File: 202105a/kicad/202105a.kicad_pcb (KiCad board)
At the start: 2 copper layers, 16 parts, among them J101 PWR, J102 IN, J103 OUT, J104 GAIN, U101 LM386

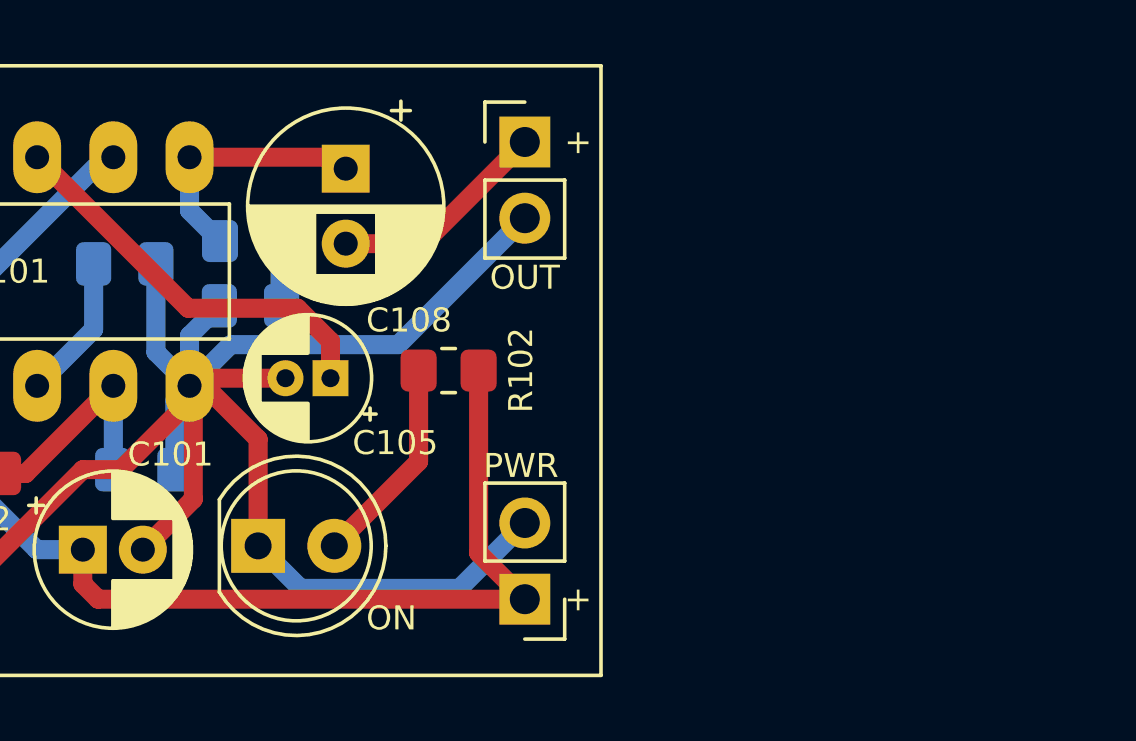
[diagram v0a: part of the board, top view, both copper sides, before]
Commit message: 添加输出插座，并移动了LED
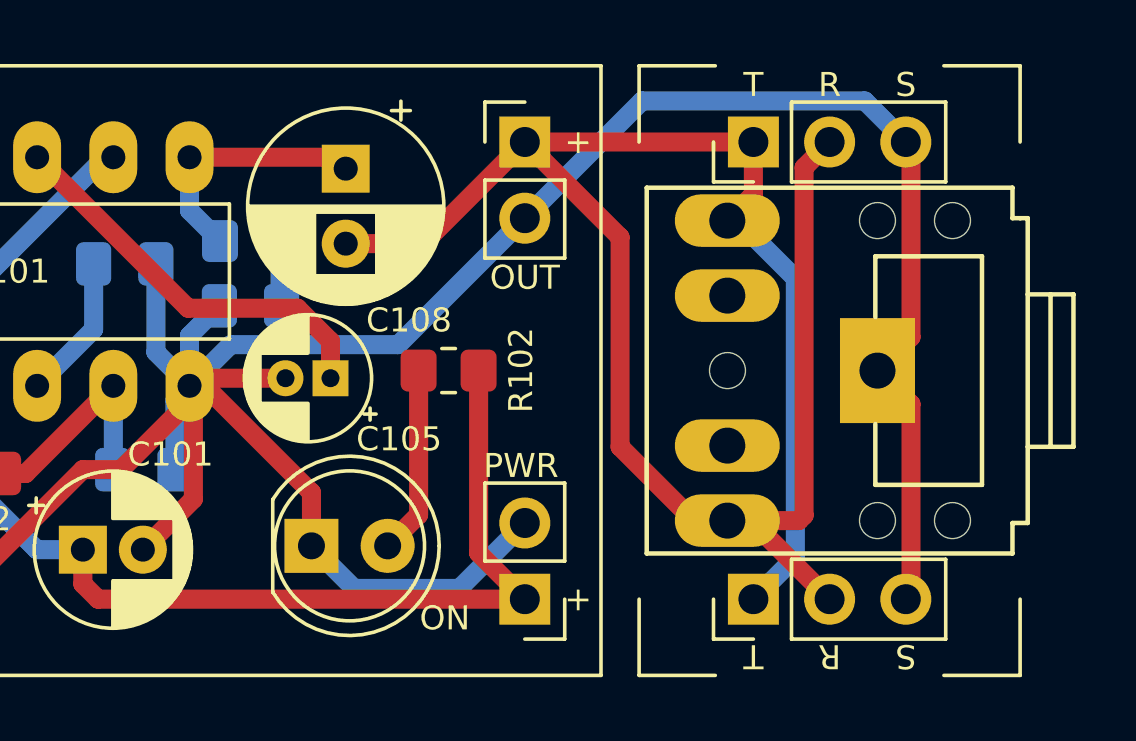
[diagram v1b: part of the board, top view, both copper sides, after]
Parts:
- added J106: OUT, bg1ren:Tayda_3.5mm_stereo_TRS_jack_A-853, F.Cu at (105.4, 114.3)
- added J107: OUT, Connector_PinHeader_2.54mm:PinHeader_1x03_P2.54mm_Vertical, F.Cu at (102.9, 121.9)
- added J108: OUT, Connector_PinHeader_2.54mm:PinHeader_1x03_P2.54mm_Vertical, F.Cu at (102.9, 106.7)
- moved D101 1.78 mm to (88.1, 120.1)
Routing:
- net /100_AF_OUT: track 7.37 -> 68.3 mm
- net /100_GND: track 65.5 -> 95.6 mm
- net Net-(D101-Pad2): track 7.01 -> 6.27 mm
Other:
- board text added: "R"
- board text added: "S"
- board text added: "T"

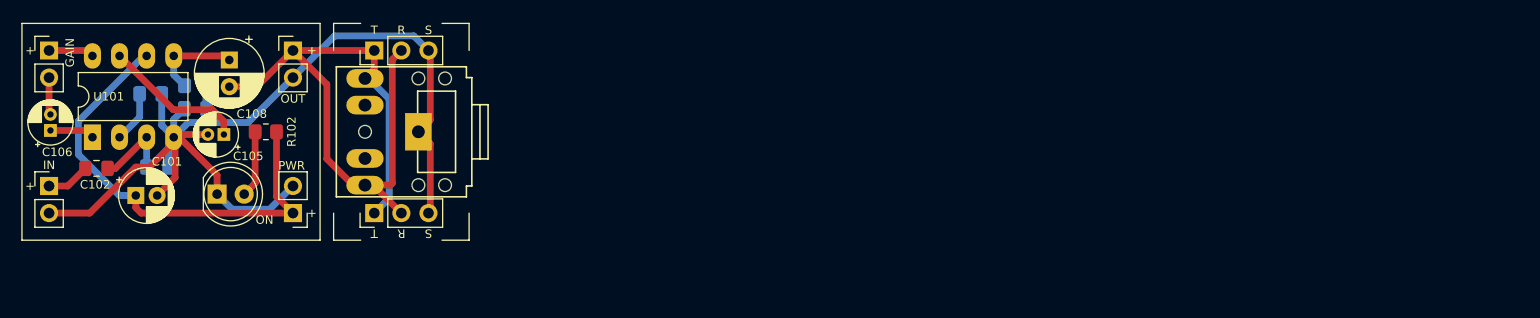
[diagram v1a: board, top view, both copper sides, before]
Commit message: 增加了FM8002A的放大器
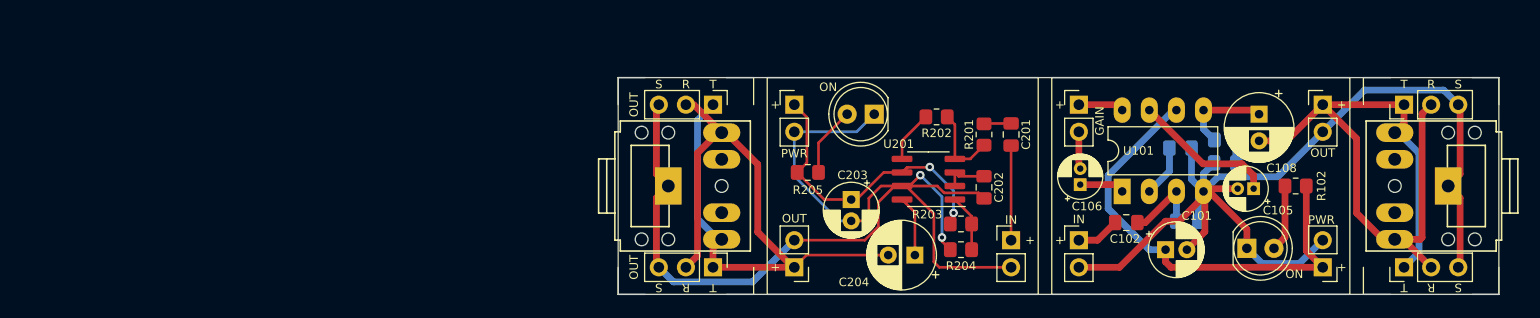
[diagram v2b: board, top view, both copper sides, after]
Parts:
- removed J108: OUT, Connector_PinHeader_2.54mm:PinHeader_1x03_P2.54mm_Vertical
- added C201: 0.39u, Capacitor_SMD:C_0805_2012Metric_Pad1.18x1.45mm_HandSolder, F.Cu at (162.6, 114.6)
- added C202: 1u, Capacitor_SMD:C_0805_2012Metric_Pad1.18x1.45mm_HandSolder, F.Cu at (160.0, 119.5)
- added C203: 100u, Capacitor_THT:CP_Radial_D5.0mm_P2.00mm, F.Cu at (147.6, 120.7)
- added C204: 470u, Capacitor_THT:CP_Radial_D6.3mm_P2.50mm, F.Cu at (153.5, 125.9)
- added D201: ON, LED_THT:LED_D5.0mm, F.Cu at (149.7, 112.6)
- added G***: LOGO, xi:xi-logo-c-05_05, B.Cu at (172.8, 125.0)
- added G***: LOGO, xi:xi-logo-c-inverted-02.5-02.5, B.Cu at (163.6, 110.7)
- added J106: OUT, Connector_PinHeader_2.54mm:PinHeader_1x03_P2.54mm_Vertical, F.Cu at (199.4, 127.0)
- added J201: PWR, Connector_PinHeader_2.54mm:PinHeader_1x02_P2.54mm_Vertical, F.Cu at (142.2, 111.8)
- added J202: IN, Connector_PinHeader_2.54mm:PinHeader_1x02_P2.54mm_Vertical, F.Cu at (162.6, 124.5)
- added J203: OUT, Connector_PinHeader_2.54mm:PinHeader_1x02_P2.54mm_Vertical, F.Cu at (142.2, 127.0)
- added J204: OUT, bg1ren:Tayda_3.5mm_stereo_TRS_jack_A-853, F.Cu at (132.0, 119.4)
- added J205: OUT, Connector_PinHeader_2.54mm:PinHeader_1x03_P2.54mm_Vertical, F.Cu at (134.6, 127.0)
- added J206: OUT, Connector_PinHeader_2.54mm:PinHeader_1x03_P2.54mm_Vertical, F.Cu at (134.6, 111.8)
- added R201: 20K, Resistor_SMD:R_0805_2012Metric_Pad1.20x1.40mm_HandSolder, F.Cu at (160.0, 114.6)
- added R202: 470K, Resistor_SMD:R_0805_2012Metric_Pad1.20x1.40mm_HandSolder, F.Cu at (155.6, 112.9)
- added R203: 0, Resistor_SMD:R_0805_2012Metric_Pad1.20x1.40mm_HandSolder, F.Cu at (157.9, 122.9)
- added R204: 0, Resistor_SMD:R_0805_2012Metric_Pad1.20x1.40mm_HandSolder, F.Cu at (157.9, 125.3)
- added R205: 22K, Resistor_SMD:R_0805_2012Metric_Pad1.20x1.40mm_HandSolder, F.Cu at (143.5, 118.1)
- added U201: FM8002A, Package_SO:SOIC-8_3.9x4.9mm_P1.27mm, F.Cu at (154.8, 118.7)
- moved J107 97.1 mm to (199.4, 111.8)
- moved C101 96.7 mm to (177.0, 125.3)
- moved C105 96.7 mm to (185.3, 119.6)
- moved C106 96.7 mm to (169.0, 119.3)
- moved C107 96.7 mm to (182.6, 117.2)
- moved J101 96.7 mm to (191.8, 127.0)
- moved J103 96.7 mm to (191.8, 111.8)
- moved J105 96.7 mm to (201.9, 119.4)
- moved R101 96.7 mm to (182.6, 115.1)
- moved C102 96.7 mm to (173.4, 122.8)
- moved C103 96.7 mm to (179.1, 122.7)
- moved C104 96.7 mm to (178.4, 115.8)
- moved J102 96.7 mm to (168.9, 124.5)
- moved J104 96.7 mm to (168.9, 111.8)
- moved R102 96.7 mm to (189.2, 119.4)
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- renumbered J106 to J105
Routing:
- net /200_GND: track 0.00 -> 105.7 mm, vias 0 -> 2
- net /200_AF_OUT: track 0.00 -> 68.6 mm
- net /200_VDD: track 0.00 -> 28.3 mm, vias 0 -> 2
- net /200_AF_IN: track 0.00 -> 8.87 mm
- net Net-(R201-Pad1): track 0.00 -> 7.50 mm
- net Net-(D201-Pad2): track 0.00 -> 6.57 mm
- net Net-(C204-Pad1): track 0.00 -> 5.71 mm
- net Net-(R203-Pad1): track 0.00 -> 5.35 mm
- net Net-(R202-Pad2): track 0.00 -> 4.86 mm
- net Net-(C202-Pad1): track 0.00 -> 4.15 mm
- net Net-(C201-Pad1): track 0.00 -> 2.56 mm
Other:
- board outline added: 82.5 x 20.3 mm
- board text added: "FM8002A Audio Amp BG1REN 20210531"
- board text added: "JLCJLCJLCJLCJLCJLCJLCJLC"
- board text added: "LM386 Audio Amp. BG1REN 20210531"
